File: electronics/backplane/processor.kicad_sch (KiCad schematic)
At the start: 13 parts, among them P6 MOLEX_PICO_PTH_VERT_2_WAY, SW1 B3U-1000P_SPST-NO_SMD, SW2 B3U-1000P_SPST-NO_SMD, X1 MICROMOD_PROCESSOR_SOCKET, X2 SWD_SMT_SOCKET

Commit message: Continue backplane
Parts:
- removed P6: MOLEX_PICO_PTH_VERT_2_WAY, Applidyne_Connector_Molex:MOLEX_PICOBLADE_53047-0210, symbol appli_connector_molex:MOLEX_PICO_PTH_VERT_2_WAY
- added SL1: SOLDER-LINK-2-TINY, Applidyne_Link:SJ1005-2N, symbol appli_link:SOLDER-LINK-2-TINY
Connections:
- net +3.3V: now also SL1.2
- net G9: now reaches X1.65 (G9/ADC_D-/CAM_HSYNC)
- net G8: now reaches X1.67 (G8)
- net G7: now reaches X1.69 (G7/BUS7)
- net G6: now reaches X1.71 (G6/BUS6)
- net at X1.72 (RTC_3V_BATT): now also SL1.1
- net G5: now reaches X1.73 (G5/BUS5)
- net 3V3_PWR_EN: no longer names the net of X1.4 (3V3_EN)
- no-connect marks 2 -> 3
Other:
- note added: "1/3rd of input voltage i.e. 1.66V for 5V input"
- note added: "3V3_EN is left NC because most MicroMod implementations don't connect any IO to it!"
- note added: "EITHER UNREGULATED 1S LiPO OR REGULATED 5V"
- note removed: "CHECK PINOUT"
- note removed: "EXTERNAL RTC BATTERY"

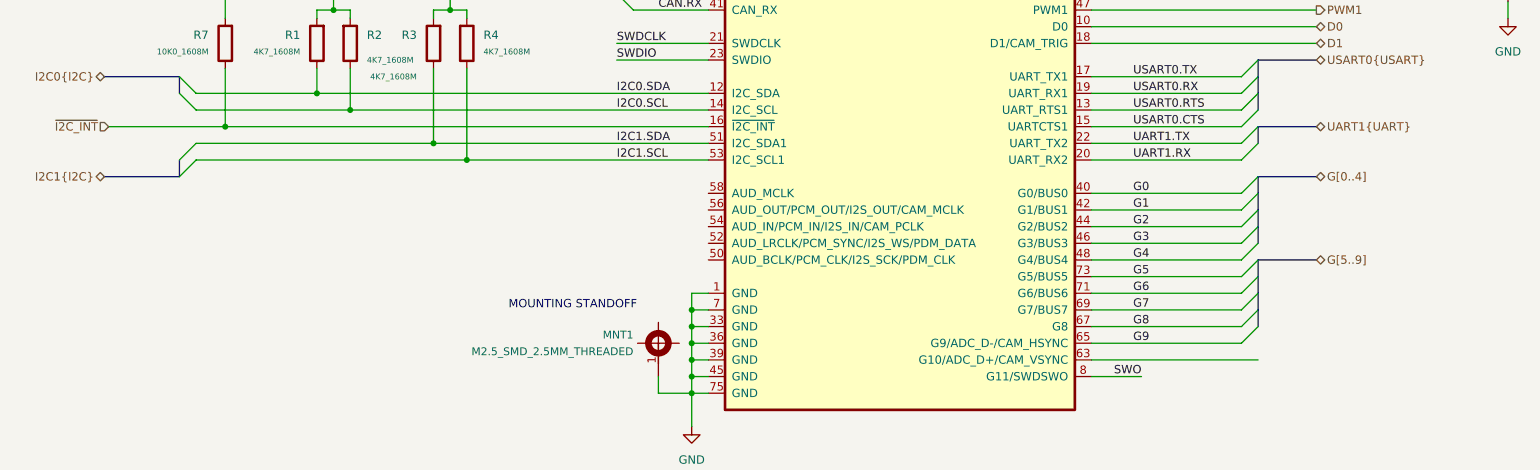
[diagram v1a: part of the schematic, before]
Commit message: Continue schematic tweaks, start routing backplane
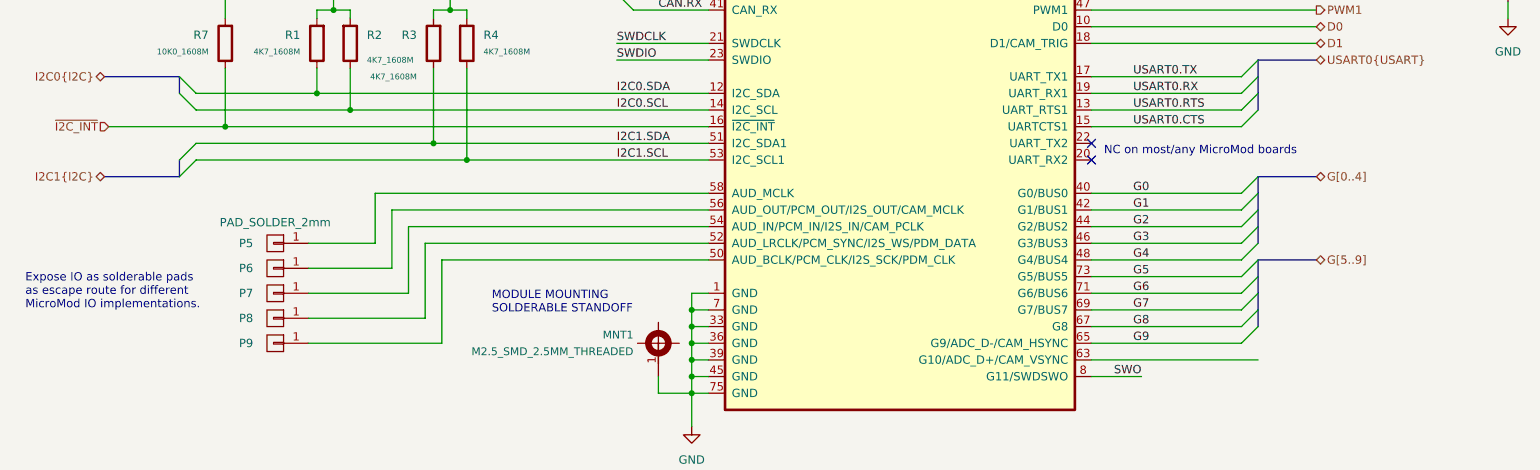
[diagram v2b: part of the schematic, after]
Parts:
- added P5, P6, P7, P8, P9: PAD_SOLDER_2mm, Applidyne_Connector:PAD_SOLDER_2mm, symbol appli_connector:PAD_SOLDER_2mm
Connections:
- net at X1.50 (AUD_BCLK/PCM_CLK/I2S_SCK/PDM_CLK): now also P9.1 (P1)
- net at X1.52 (AUD_LRCLK/PCM_SYNC/I2S_WS/PDM_DATA): now also P8.1 (P1)
- net at X1.54 (AUD_IN/PCM_IN/I2S_IN/CAM_PCLK): now also P7.1 (P1)
- net at X1.56 (AUD_OUT/PCM_OUT/I2S_OUT/CAM_MCLK): now also P6.1 (P1)
- net at X1.58 (AUD_MCLK): now also P5.1 (P1)
- net UART1.RX: no longer names the net of X1.20 (UART_RX2)
- net UART1.TX: no longer names the net of X1.22 (UART_TX2)
- no-connect marks 3 -> 5
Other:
- note added: "Expose IO as solderable pads as escape route for different MicroMod IO implementations."
- note added: "MODULE MOUNTING SOLDERABLE STANDOFF"
- note added: "NC on most/any MicroMod boards"
- note removed: "MOUNTING STANDOFF"

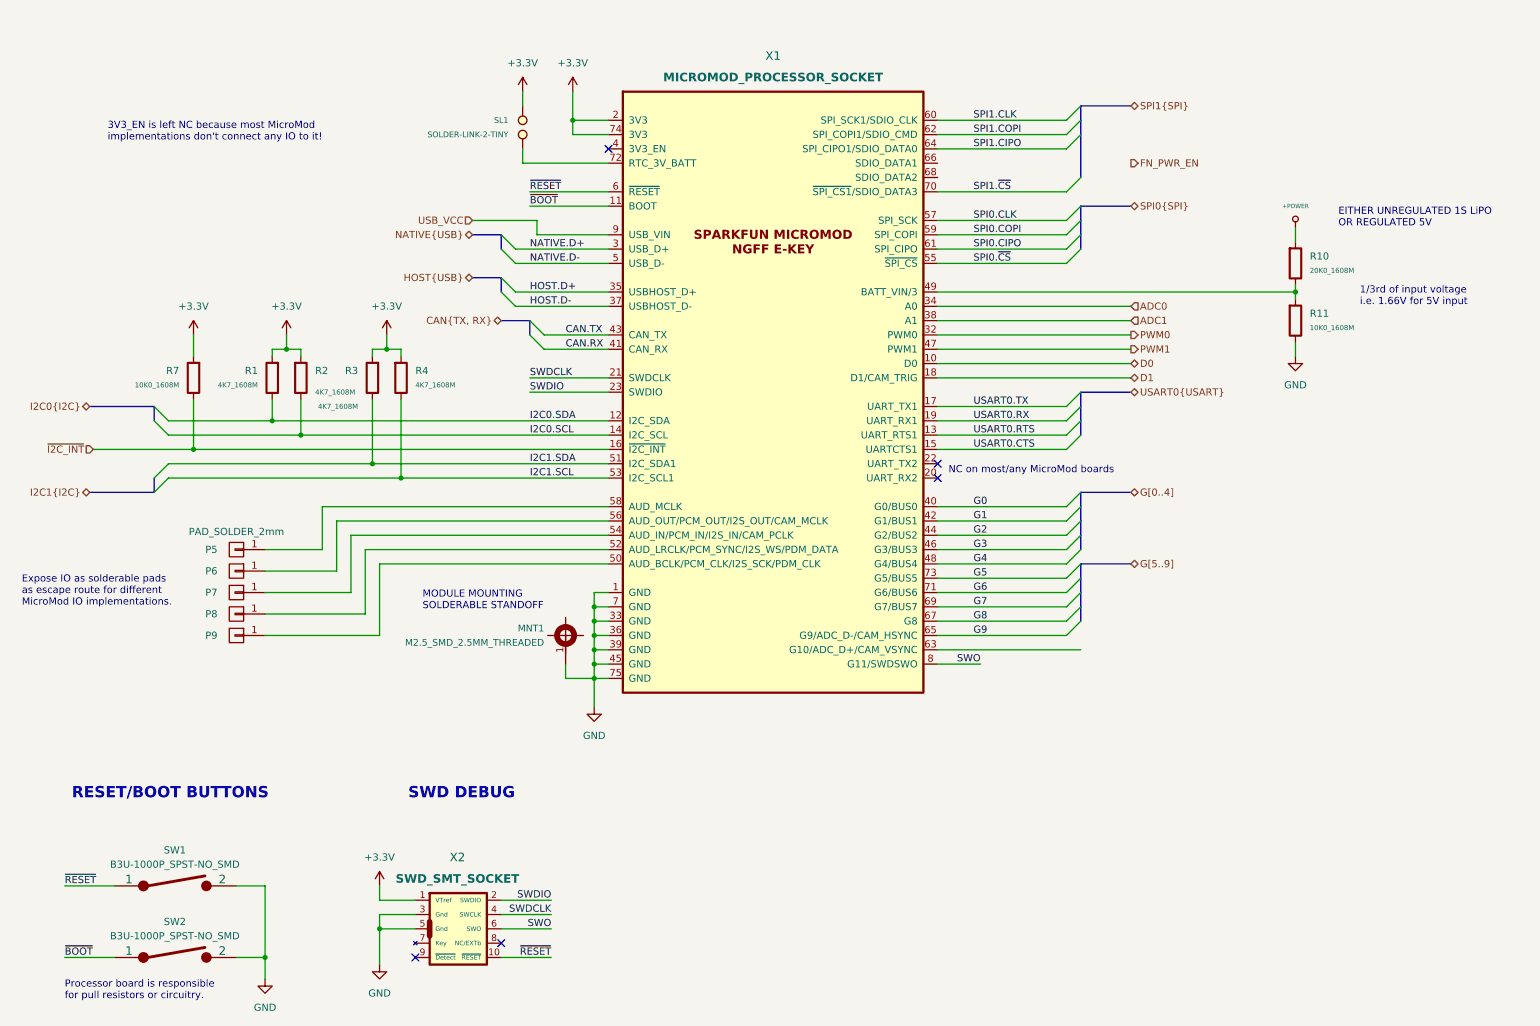
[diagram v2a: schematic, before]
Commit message: Continue backplane design Cleanup schematic, most routing and placement done
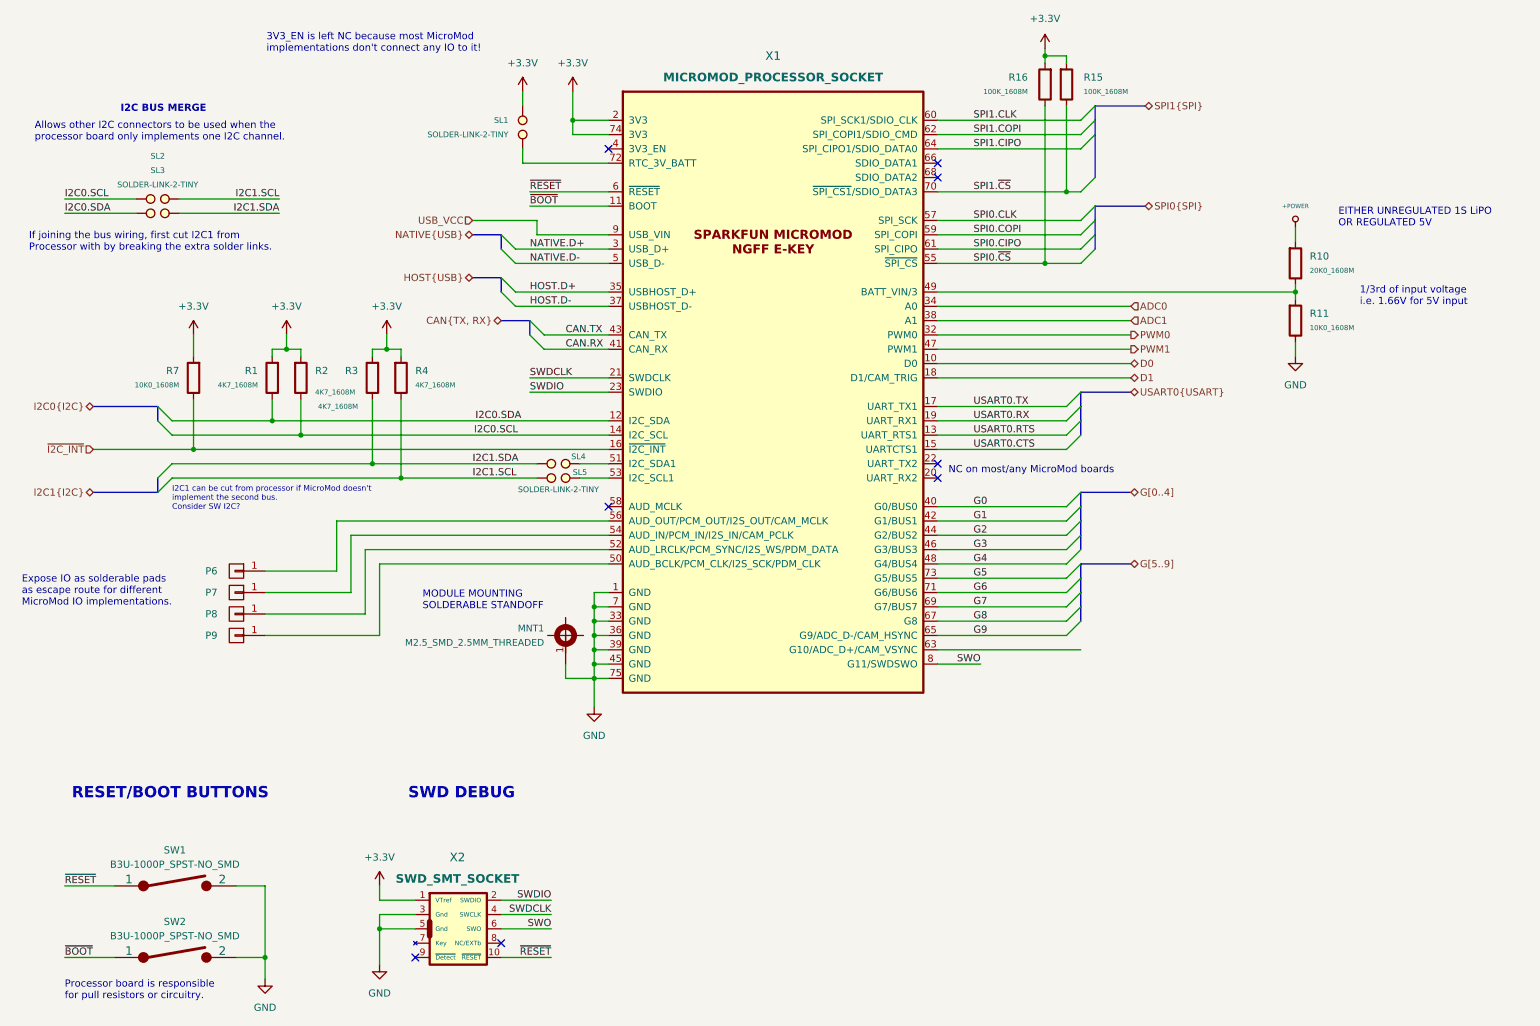
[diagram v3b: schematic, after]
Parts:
- removed P5: PAD_SOLDER_2mm, Applidyne_Connector:PAD_SOLDER_2mm, symbol appli_connector:PAD_SOLDER_2mm
- added R15, R16: 100K_1608M, Applidyne_Resistor:RESC1608X50N, symbol appli_resistor:100K_1608M
- added SL2, SL3, SL4, SL5: SOLDER-LINK-2-TINY, Applidyne_Link:SJ1005-2N, symbol appli_link:SOLDER-LINK-2-TINY
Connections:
- net +3.3V: now also R15.1, R16.1
- net I2C0.SCL: now also SL2.1
- net I2C0.SDA: now also SL3.2
- net I2C1.SCL: now also SL2.2, SL5.1; no longer X1.53 (I2C_SCL1)
- net I2C1.SDA: now also SL3.1, SL4.1; no longer X1.51 (I2C_SDA1)
- net SPI0.~{CS}: now also R16.2
- net SPI1.~{CS}: now also R15.2
- new net: SL4.2, X1.51 (I2C_SDA1)
- new net: SL5.2, X1.53 (I2C_SCL1)
- no-connect marks 5 -> 8
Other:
- note added: "Allows other I2C connectors to be used when the processor board only implements one I2C channel."
- note added: "I2C BUS MERGE"
- note added: "I2C1 can be cut from processor if MicroMod doesn't implement the second bus. Consider SW I2C?"
- note added: "If joining the bus wiring, first cut I2C1 from Processor with by breaking the extra solder links."
